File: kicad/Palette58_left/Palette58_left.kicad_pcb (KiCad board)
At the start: 2 copper layers, 145 x 127.8 mm, 131 parts, among them SW1 MSK12C02-HB, SW2 TS-1187A-B-A-B

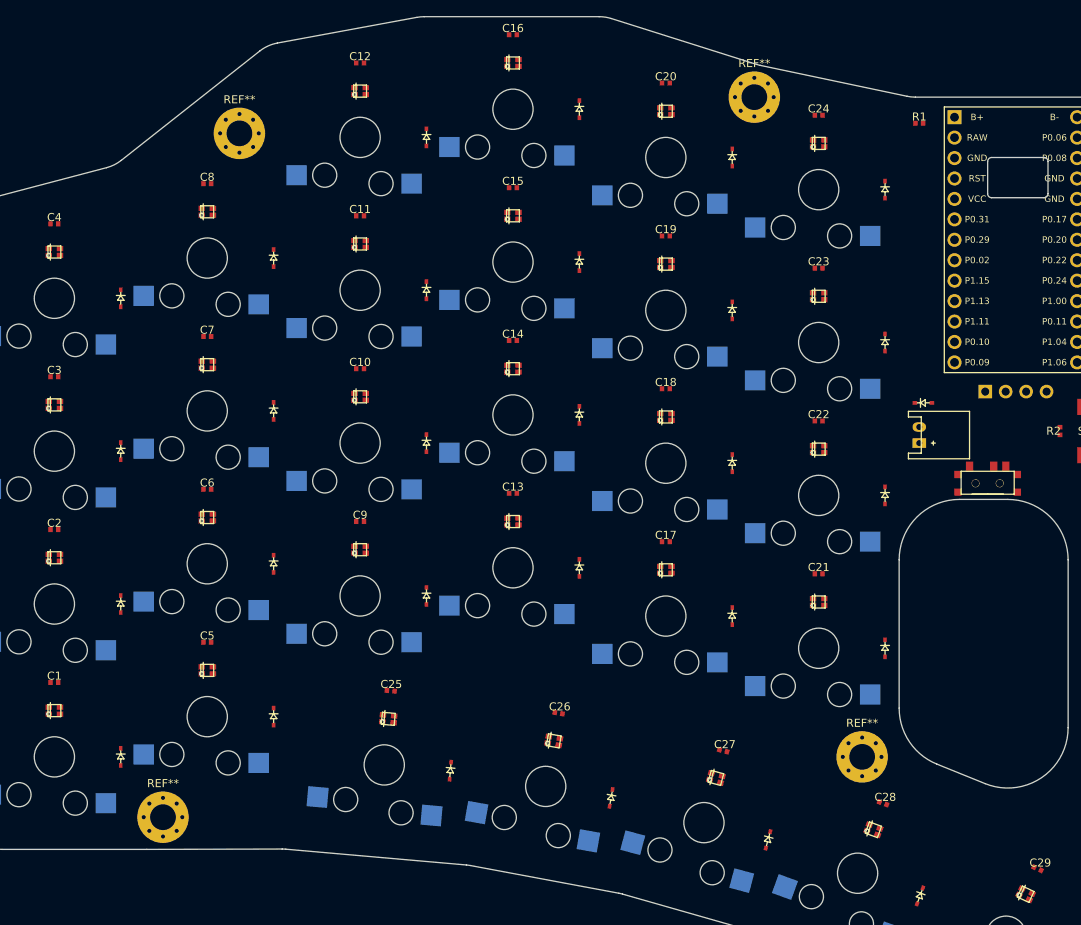
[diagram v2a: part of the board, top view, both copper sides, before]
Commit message: fix: add vias back to left half hotswap pads
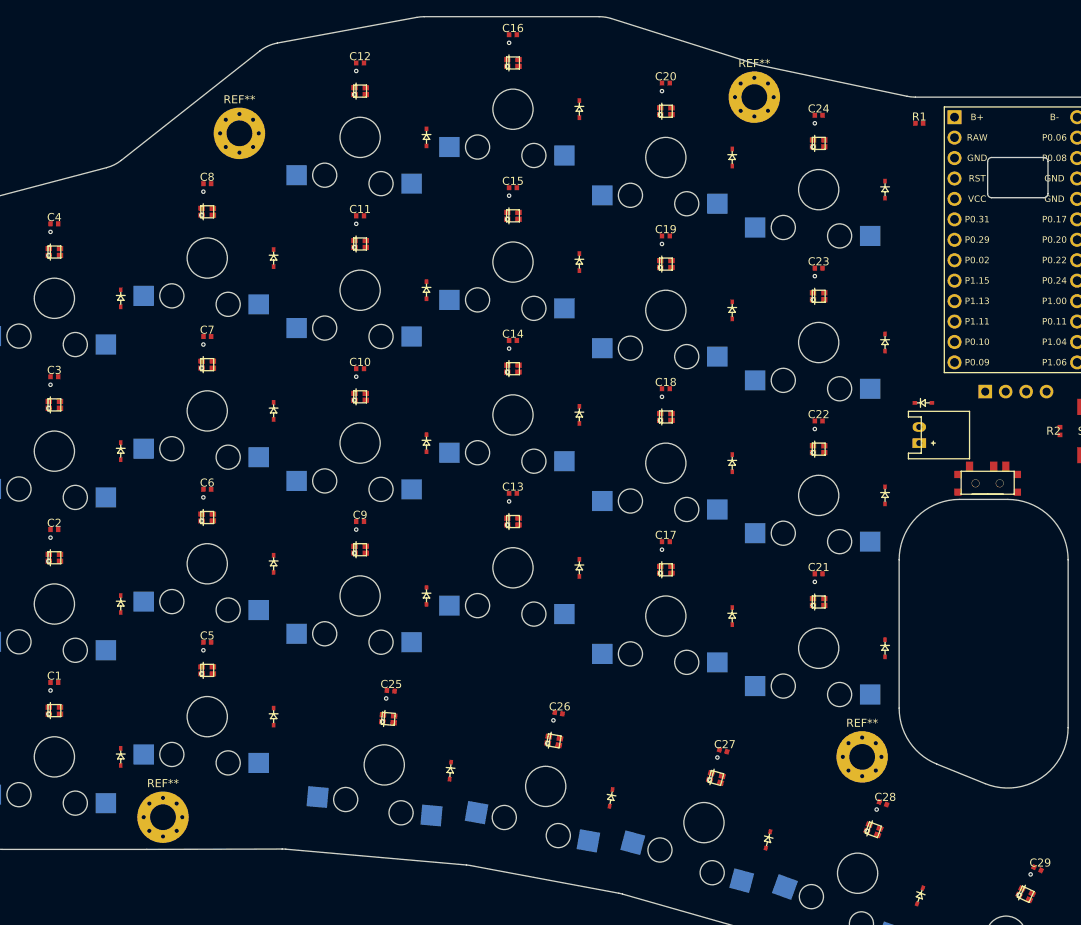
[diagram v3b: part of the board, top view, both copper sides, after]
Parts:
- removed _34, _35, _36: , ToolingHole
- added _63: , ToolingHole, F.Cu at (-8.50, -65.5)
- added _64: , ToolingHole, F.Cu at (-8.50, 8.50)
- added _65: , ToolingHole, F.Cu at (122.4, 33.6)
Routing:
- net GND: vias 29 -> 58
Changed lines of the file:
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@@
+      (net 43)
+    )
+    (via
+      (at -0.48 -8.25)
+      (size 0.56)
+      (layers "F.Cu" "B.Cu")
+      (net 43)
+    )
+    (via
+      (at -0.48 -27.25)
+      (size 0.56)
+      (layers "F.Cu" "B.Cu")
+      (net 43)
+    )
+    (via
+      (at -0.48 -46.25)
+      (size 0.56)
+      (layers "F.Cu" "B.Cu")
+      (net 43)
+    )
+    (via
+      (at -0.48 -65.25)
+      (size 0.56)
+      (layers "F.Cu" "B.Cu")
+      (net 43)
+    )
+    (via
+      (at 18.52 -13.25)
+      (size 0.56)
+      (layers "F.Cu" "B.Cu")
+      (net 43)
+    )
+    (via
+      (at 18.52 -32.25)
+      (size 0.56)
+      (layers "F.Cu" "B.Cu")
+      (net 43)
+    )
+    (via
+      (at 18.52 -51.25)
+      (size 0.56)
+      (layers "F.Cu" "B.Cu")
+      (net 43)
+    )
+    (via
+      (at 18.52 -70.25)
+      (size 0.56)
+      (layers "F.Cu" "B.Cu")
+      (net 43)
+    )
+    (via
+      (at 37.52 -28.25)
+      (size 0.56)
+      (layers "F.Cu" "B.Cu")
+      (net 43)
+    )
+    (via
+      (at 37.52 -47.25)
+      (size 0.56)
+      (layers "F.Cu" "B.Cu")
+      (net 43)
+    )
+    (via
+      (at 37.52 -66.25)
+      (size 0.56)
+      (layers "F.Cu" "B.Cu")
+      (net 43)
+    )
+    (via
+      (at 37.52 -85.25)
+      (size 0.56)
+      (layers "F.Cu" "B.Cu")
+      (net 43)
+    )
+    (via
+      (at 56.52 -31.75)
+      (size 0.56)
+      (layers "F.Cu" "B.Cu")
+      (net 43)
+    )
+    (via
+      (at 56.52 -50.75)
+      (size 0.56)
+      (layers "F.Cu" "B.Cu")
+      (net 43)
+    )
+    (via
+      (at 56.52 -69.75)
+      (size 0.56)
+      (layers "F.Cu" "B.Cu")
+      (net 43)
+    )
+    (via
+      (at 56.52 -88.75)
+      (size 0.56)
+      (layers "F.Cu" "B.Cu")
+      (net 43)
+    )
+    (via
+      (at 75.52 -25.75)
+      (size 0.56)
+      (layers "F.Cu" "B.Cu")
+      (net 43)
+    )
+    (via
+      (at 75.52 -44.75)
+      (size 0.56)
+      (layers "F.Cu" "B.Cu")
+      (net 43)
+    )
+    (via
+      (at 75.52 -63.75)
+      (size 0.56)
+      (layers "F.Cu" "B.Cu")
+      (net 43)
+    )
+    (via
+      (at 75.52 -82.75)
+      (size 0.56)
+      (layers "F.Cu" "B.Cu")
+      (net 43)
+    )
+    (via
+      (at 94.52 -21.75)
+      (size 0.56)
+      (layers "F.Cu" "B.Cu")
+      (net 43)
+    )
+    (via
+      (at 94.52 -40.75)
+      (size 0.56)
+      (layers "F.Cu" "B.Cu")
+      (net 43)
+    )
+    (via
+      (at 94.52 -59.75)
+      (size 0.56)
+      (layers "F.Cu" "B.Cu")
+      (net 43)
+    )
+    (via
+      (at 94.52 -78.75)
+      (size 0.56)
+      (layers "F.Cu" "B.Cu")
+      (net 43)
+    )
+    (via
+      (at 41.2408614 -7.260441)
+      (size 0.56)
+      (layers "F.Cu" "B.Cu")
+      (net 43)
+    )
+    (via
+      (at 62.0289205 -4.538467200000001)
+      (size 0.56)
+      (layers "F.Cu" "B.Cu")
+      (net 43)
+    )
+    (via
+      (at 82.4079559 0.08056409999999836)
+      (size 0.56)
+      (layers "F.Cu" "B.Cu")
+      (net 43)
+    )
+    (via
+      (at 102.20620390000002 6.545343299999999)
+      (size 0.56)
+      (layers "F.Cu" "B.Cu")
+      (net 43)
+    )
+    (via
+      (at 121.34231570000001 14.607861399999997)
+      (size 0.56)
+      (layers "F.Cu" "B.Cu")
       (net 43)
     )
@@
   (module ToolingHole (layer F.Cu)
     (at -8.5 -65.5 0)
-    (property "Reference" _34
+    (property "Reference" _63
       (at 0 0)
       (layer F.SilkS)
@@
   (module ToolingHole (layer F.Cu)
     (at -8.5 8.5 0)
-    (property "Reference" _35
+    (property "Reference" _64
       (at 0 0)
       (layer F.SilkS)
@@
   (module ToolingHole (layer F.Cu)
     (at 122.40210380000002 33.5836288 -25)
-    (property "Reference" _36
+    (property "Reference" _65
       (at 0 0)
       (layer F.SilkS)

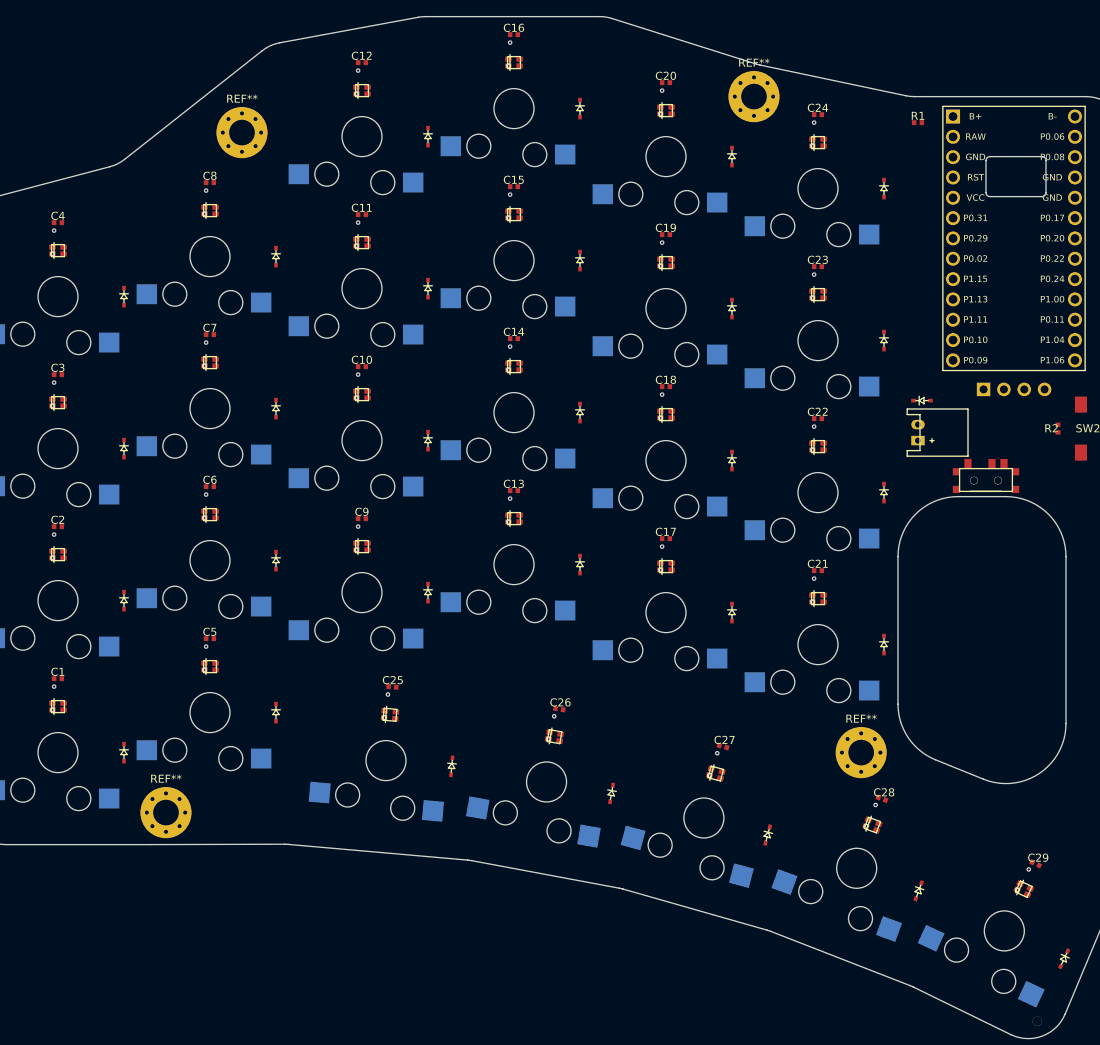
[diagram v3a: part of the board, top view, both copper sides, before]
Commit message: fix: fix capacitor and via placement
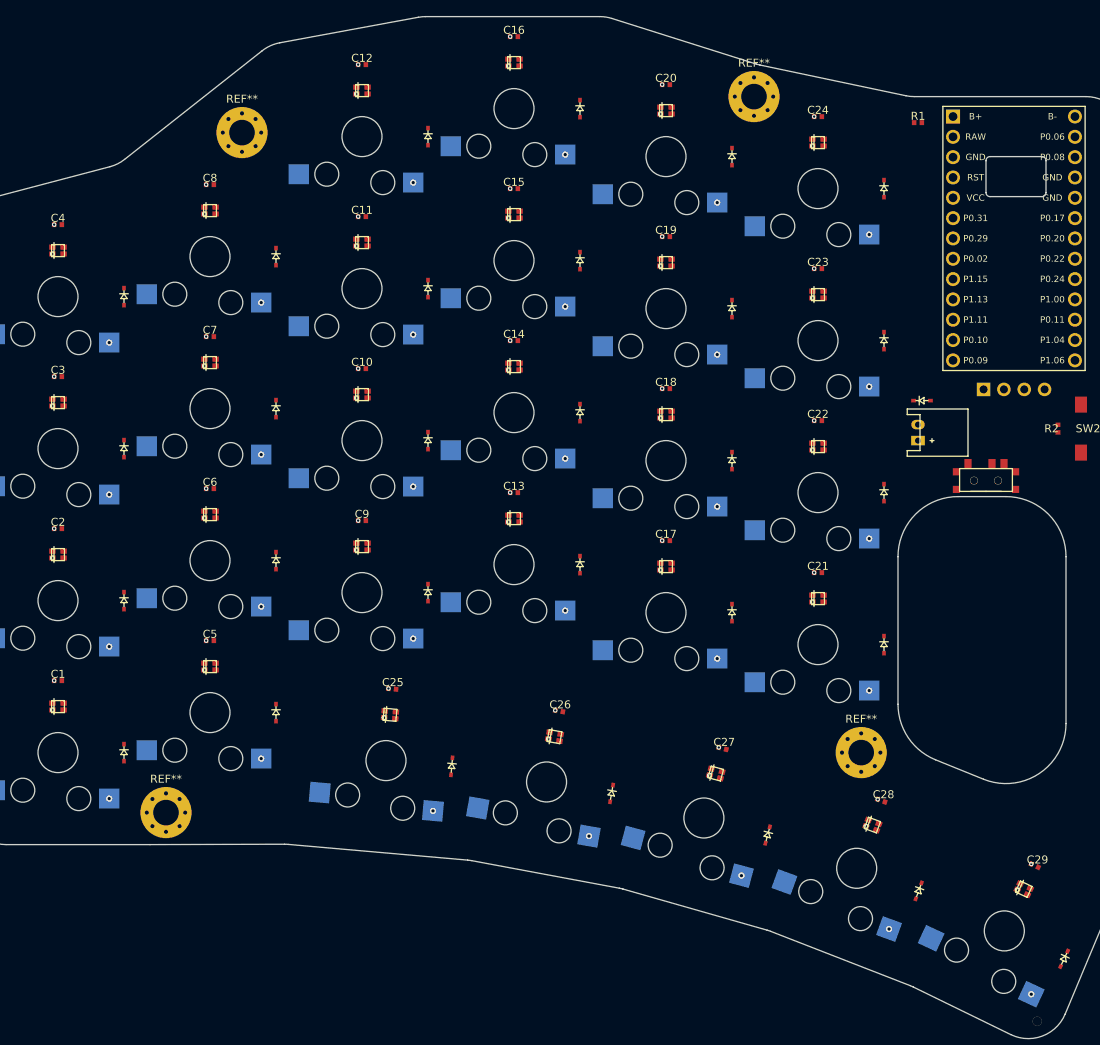
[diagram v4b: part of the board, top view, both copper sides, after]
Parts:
- removed _63, _64, _65: , ToolingHole
- added _92: , ToolingHole, F.Cu at (-8.50, -65.5)
- added _93: , ToolingHole, F.Cu at (-8.50, 8.50)
- added _94: , ToolingHole, F.Cu at (122.4, 33.6)
- moved C27 0.25 mm to (83.1, -0.52)
- moved C25 0.25 mm to (41.8, -7.97)
- moved C1 0.25 mm to (0.00, -9.00)
- moved C10 0.25 mm to (38.0, -48.0)
- moved C11 0.25 mm to (38.0, -67.0)
- moved C12 0.25 mm to (38.0, -86.0)
- moved C13 0.25 mm to (57.0, -32.5)
- moved C14 0.25 mm to (57.0, -51.5)
- moved C15 0.25 mm to (57.0, -70.5)
- moved C16 0.25 mm to (57.0, -89.5)
- moved C17 0.25 mm to (76.0, -26.5)
- moved C18 0.25 mm to (76.0, -45.5)
- moved C19 0.25 mm to (76.0, -64.5)
- moved C2 0.25 mm to (0.00, -28.0)
- moved C20 0.25 mm to (76.0, -83.5)
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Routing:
- net ring_top: vias 0 -> 1
- net ring_num: vias 0 -> 1
- net ring_home: vias 0 -> 1
- net ring_bottom: vias 0 -> 1
- net pinky_top: vias 0 -> 1
- net pinky_num: vias 0 -> 1
- net pinky_home: vias 0 -> 1
- net pinky_bottom: vias 0 -> 1
- net outer_top: vias 0 -> 1
- net outer_num: vias 0 -> 1
- net outer_home: vias 0 -> 1
- net outer_cluster: vias 0 -> 1
- net outer_bottom: vias 0 -> 1
- net outer-3_cluster: vias 0 -> 1
- net outer-2_cluster: vias 0 -> 1
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
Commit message: Send left half for production
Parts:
- added G***: LOGO, Palette58:logo, F.Cu at (129.8, -13.6)
- LED1, LED10, LED11, LED12, LED13, LED14, LED15, LED16, LED17, LED18, LED19, LED2, LED20, LED21, LED22, LED23, LED24, LED25, LED26, LED27, LED28, LED29, LED3, LED4, LED5, LED6, LED7, LED8, LED9: value (none) -> XINGLIGHTXL-1615RGBC-WS2812B; footprint WS2812B -> LED_SMD:XINGLIGHT XL-1615RGBC-WS2812B
- R1: footprint Resistor -> Resistor_SMD:R_0402_1005Metric
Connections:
- LED1 pad 1: (no net) -> VCC
- LED1 pad 2: GND -> Net-(LED1-DOUT)
- LED1 pad 3: (no net) -> GND
- LED1 pad 4: VCC -> Net-(LED1-DIN)
- LED10 pad 1: (no net) -> VCC
- LED10 pad 2: GND -> Net-(LED10-DOUT)
- LED10 pad 3: (no net) -> GND
- LED10 pad 4: VCC -> Net-(LED10-DIN)
- LED11 pad 1: (no net) -> VCC
- LED11 pad 2: GND -> Net-(LED11-DOUT)
- LED11 pad 3: (no net) -> GND
- LED11 pad 4: VCC -> Net-(LED11-DIN)
- LED12 pad 1: (no net) -> VCC
- LED12 pad 2: GND -> Net-(LED12-DOUT)
- LED12 pad 3: (no net) -> GND
- LED12 pad 4: VCC -> Net-(LED12-DIN)
- LED13 pad 1: (no net) -> VCC
- LED13 pad 2: GND -> Net-(LED13-DOUT)
- LED13 pad 3: (no net) -> GND
- LED13 pad 4: VCC -> Net-(LED13-DIN)
- LED14 pad 1: (no net) -> VCC
- LED14 pad 2: GND -> Net-(LED10-DIN)
- LED14 pad 3: (no net) -> GND
- LED14 pad 4: VCC -> Net-(LED14-DIN)
- LED15 pad 1: (no net) -> VCC
- LED15 pad 2: GND -> Net-(LED15-DOUT)
- LED15 pad 3: (no net) -> GND
- LED15 pad 4: VCC -> Net-(LED11-DOUT)
- LED16 pad 1: (no net) -> VCC
- LED16 pad 2: GND -> Net-(LED12-DIN)
- LED16 pad 3: (no net) -> GND
- LED16 pad 4: VCC -> Net-(LED16-DIN)
- LED17 pad 1: (no net) -> VCC
- LED17 pad 2: GND -> Net-(LED17-DOUT)
- LED17 pad 3: (no net) -> GND
- LED17 pad 4: VCC -> Net-(LED13-DOUT)
- LED18 pad 1: (no net) -> VCC
- LED18 pad 2: GND -> Net-(LED14-DIN)
- LED18 pad 3: (no net) -> GND
- LED18 pad 4: VCC -> Net-(LED18-DIN)
- LED19 pad 1: (no net) -> VCC
- LED19 pad 2: GND -> Net-(LED19-DOUT)
- LED19 pad 3: (no net) -> GND
- LED19 pad 4: VCC -> Net-(LED15-DOUT)
- LED2 pad 1: (no net) -> VCC
- LED2 pad 2: GND -> Net-(LED1-DIN)
- LED2 pad 3: (no net) -> GND
- LED2 pad 4: VCC -> Net-(LED2-DIN)
- LED20 pad 1: (no net) -> VCC
- LED20 pad 2: GND -> Net-(LED16-DIN)
- LED20 pad 3: (no net) -> GND
- LED20 pad 4: VCC -> Net-(LED20-DIN)
- LED21 pad 1: (no net) -> VCC
- LED21 pad 2: GND -> Net-(LED21-DOUT)
- LED21 pad 3: (no net) -> GND
- LED21 pad 4: VCC -> Net-(LED17-DOUT)
- LED22 pad 1: (no net) -> VCC
- LED22 pad 2: GND -> Net-(LED18-DIN)
- LED22 pad 3: (no net) -> GND
- LED22 pad 4: VCC -> Net-(LED22-DIN)
- LED23 pad 1: (no net) -> VCC
- LED23 pad 2: GND -> Net-(LED22-DIN)
- LED23 pad 3: (no net) -> GND
- LED23 pad 4: VCC -> Net-(LED19-DOUT)
- LED24 pad 1: (no net) -> VCC
- LED24 pad 2: GND -> Net-(LED20-DIN)
- LED24 pad 3: (no net) -> GND
- LED24 pad 4: VCC -> Net-(LED24-DIN)
- LED25 pad 1: (no net) -> VCC
- LED25 pad 2: GND -> Net-(LED25-DOUT)
- LED25 pad 3: (no net) -> GND
- LED25 pad 4: VCC -> Net-(LED21-DOUT)
- LED26 pad 1: (no net) -> VCC
- LED26 pad 2: GND -> Net-(LED26-DOUT)
- LED26 pad 3: (no net) -> GND
- LED26 pad 4: VCC -> Net-(LED25-DOUT)
- LED27 pad 1: (no net) -> VCC
- LED27 pad 2: GND -> Net-(LED27-DOUT)
- LED27 pad 3: (no net) -> GND
- LED27 pad 4: VCC -> Net-(LED26-DOUT)
- LED28 pad 1: (no net) -> VCC
- LED28 pad 2: GND -> Net-(LED28-DOUT)
- LED28 pad 3: (no net) -> GND
- LED28 pad 4: VCC -> Net-(LED27-DOUT)
- LED29 pad 1: (no net) -> VCC
- LED29 pad 2: GND -> unconnected-(LED29-DOUT-Pad2)
- LED29 pad 3: (no net) -> GND
- LED29 pad 4: VCC -> Net-(LED28-DOUT)
- LED3 pad 1: (no net) -> VCC
- LED3 pad 2: GND -> Net-(LED3-DOUT)
- LED3 pad 3: (no net) -> GND
- LED3 pad 4: VCC -> Net-(LED3-DIN)
- LED4 pad 1: (no net) -> VCC
- LED4 pad 2: GND -> Net-(LED3-DIN)
- LED4 pad 3: (no net) -> GND
- LED4 pad 4: VCC -> Net-(LED4-DIN)
- LED5 pad 1: (no net) -> VCC
- LED5 pad 2: GND -> Net-(LED5-DOUT)
- LED5 pad 3: (no net) -> GND
- LED5 pad 4: VCC -> Net-(LED1-DOUT)
- LED6 pad 1: (no net) -> VCC
- LED6 pad 2: GND -> Net-(LED2-DIN)
- LED6 pad 3: (no net) -> GND
- LED6 pad 4: VCC -> Net-(LED10-DOUT)
- LED7 pad 1: (no net) -> VCC
- LED7 pad 2: GND -> Net-(LED11-DIN)
- LED7 pad 3: (no net) -> GND
- LED7 pad 4: VCC -> Net-(LED3-DOUT)
- LED8 pad 1: (no net) -> VCC
- LED8 pad 2: GND -> Net-(LED4-DIN)
- LED8 pad 3: (no net) -> GND
- LED8 pad 4: VCC -> Net-(LED12-DOUT)
- LED9 pad 1: (no net) -> VCC
- LED9 pad 2: GND -> Net-(LED13-DIN)
- LED9 pad 3: (no net) -> GND
- LED9 pad 4: VCC -> Net-(LED5-DOUT)
- R1 pad 1: (no net) -> Net-(LED24-DIN)
- R1 pad 2: (no net) -> P0.06
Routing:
- net col_2: track 0.00 -> 198.0 mm
- net col_1: track 0.00 -> 197.4 mm
- net col_3: track 0.00 -> 188.2 mm
- net row_5: track 0.00 -> 185.0 mm, vias 0 -> 2
- net row_4: track 0.00 -> 177.4 mm
- net col_4: track 0.00 -> 165.2 mm, vias 0 -> 4
- net row_3: track 0.00 -> 161.0 mm
- net col_5: track 0.00 -> 148.2 mm, vias 0 -> 2
- net row_2: track 0.00 -> 144.4 mm
- net row_1: track 0.00 -> 137.7 mm
- net col_6: track 0.00 -> 127.1 mm
- net Net-(LED21-DOUT): track 0.00 -> 62.8 mm, vias 0 -> 4
- net RST: track 0.00 -> 60.7 mm
- net B+: track 0.00 -> 50.1 mm, vias 0 -> 1
- net Net-(LED15-DOUT): track 0.00 -> 30.0 mm, vias 0 -> 2
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- added copper zone on B.Cu, net GND
- added copper zone on F.Cu, net VCC
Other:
- net class Default removed
- board text added: "JLCJLCJLC"

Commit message: Simplify left half
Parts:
- removed C1, C10, C11, C12, C13, C14, C15, C16, C17, C18, C19, C2, C20, C21, C22, C23, C24, C25, C26, C27, C28, C29, C3, C4, C5, C6, C7, C8, C9: 100nF, Capacitor
- removed D30: 1N5819, ComboDiode
- removed LED1, LED10, LED11, LED12, LED13, LED14, LED15, LED16, LED17, LED18, LED19, LED2, LED20, LED21, LED22, LED23, LED24, LED25, LED26, LED27, LED28, LED29, LED3, LED4, LED5, LED6, LED7, LED8, LED9: XINGLIGHTXL-1615RGBC-WS2812B, LED_SMD:XINGLIGHT XL-1615RGBC-WS2812B
- removed R1: 330Ω, Resistor_SMD:R_0402_1005Metric
- removed R2: 10kΩ, Resistor
- removed the REF** at (100.4, 0.00)
- removed the REF** at (23.0, -77.5)
- removed the REF** at (13.5, 7.50)
- removed the REF** at (87.0, -82.0)
- removed _92, _93, _94: , ToolingHole
- added REF**: MountingHole_3.2mm_M3_Pad_Via, MountingHole:MountingHole_3.2mm_M3_Pad_Via, F.Cu at (71.5, 47.2)
- added REF**: MountingHole_3.2mm_M3_Pad_Via, MountingHole:MountingHole_3.2mm_M3_Pad_Via, F.Cu at (148.8, 123.7)
- added REF**: MountingHole_3.2mm_M3_Pad_Via, MountingHole:MountingHole_3.2mm_M3_Pad_Via, F.Cu at (62.0, 131.2)
- added REF**: MountingHole_3.2mm_M3_Pad_Via, MountingHole:MountingHole_3.2mm_M3_Pad_Via, F.Cu at (135.4, 42.2)
- added _34: , ToolingHole, F.Cu at (40.0, 58.2)
- added _35: , ToolingHole, F.Cu at (40.0, 132.2)
- added _36: , ToolingHole, F.Cu at (170.9, 157.3)
- moved SW2 133.4 mm to (177.4, 84.2)
- moved G*** 133.0 mm to (178.2, 110.3)
- moved D1 132.8 mm to (56.7, 123.7)
- moved D10 132.8 mm to (94.7, 84.7)
- moved D11 132.8 mm to (94.7, 65.7)
- moved D12 132.8 mm to (94.7, 46.7)
- moved D13 132.8 mm to (113.7, 100.2)
- moved D14 132.8 mm to (113.7, 81.2)
- moved D15 132.8 mm to (113.7, 62.2)
- moved D16 132.8 mm to (113.7, 43.2)
- moved D17 132.8 mm to (132.7, 106.2)
- moved D18 132.8 mm to (132.7, 87.2)
- moved D19 132.8 mm to (132.7, 68.2)
- moved D2 132.8 mm to (56.7, 104.7)
- moved D20 132.8 mm to (132.7, 49.2)
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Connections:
- MCU1 pad 19: row_1 -> SDA
- MCU1 pad 20: row_2 -> SCL
- MCU1 pad 21: row_3 -> row_1
- MCU1 pad 22: row_4 -> row_2
- MCU1 pad 23: row_5 -> row_3
- MCU1 pad 24: P0.11 -> row_4
- MCU1 pad 25: SCL -> row_5
- MCU1 pad 26: SDA -> P1.06
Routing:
- net Net-(LED21-DOUT): track 62.8 -> 0.00 mm, vias 4 -> 0
- net Net-(LED15-DOUT): track 30.0 -> 0.00 mm, vias 2 -> 0
- net Net-(LED11-DIN): track 29.9 -> 0.00 mm, vias 2 -> 0
- net Net-(LED5-DOUT): track 29.7 -> 0.00 mm, vias 2 -> 0
- net Net-(LED19-DOUT): track 29.2 -> 0.00 mm, vias 2 -> 0
- net VCC: track 0.00 -> 29.0 mm, vias 0 -> 3
- net Net-(LED22-DIN): track 28.3 -> 0.00 mm, vias 2 -> 0
- net Net-(LED1-DIN): track 28.1 -> 0.00 mm
- net Net-(LED13-DOUT): track 28.0 -> 0.00 mm, vias 2 -> 0
- net Net-(LED17-DOUT): track 27.8 -> 0.00 mm, vias 2 -> 0
- net Net-(LED3-DIN): track 27.7 -> 0.00 mm
- net Net-(LED25-DOUT): track 25.7 -> 0.00 mm
- net Net-(LED1-DOUT): track 25.5 -> 0.00 mm, vias 2 -> 0
- net Net-(LED26-DOUT): track 25.0 -> 0.00 mm
- net Net-(LED28-DOUT): track 25.0 -> 0.00 mm
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- added copper zone on F.Cu, net GND
- removed copper zone on F.Cu, net VCC
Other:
- outline, holes or cut-outs redrawn
- board text removed: "JLCJLCJLC"
